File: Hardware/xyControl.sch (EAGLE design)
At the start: 72 parts, among them IC1 ATMEGA2560-16AU, IC2 74HC573D, IC3 K6X4008C1FSMD, IC4 FT232RL, Q7 16M, T1 0-XYTHOBUZ_TASTER

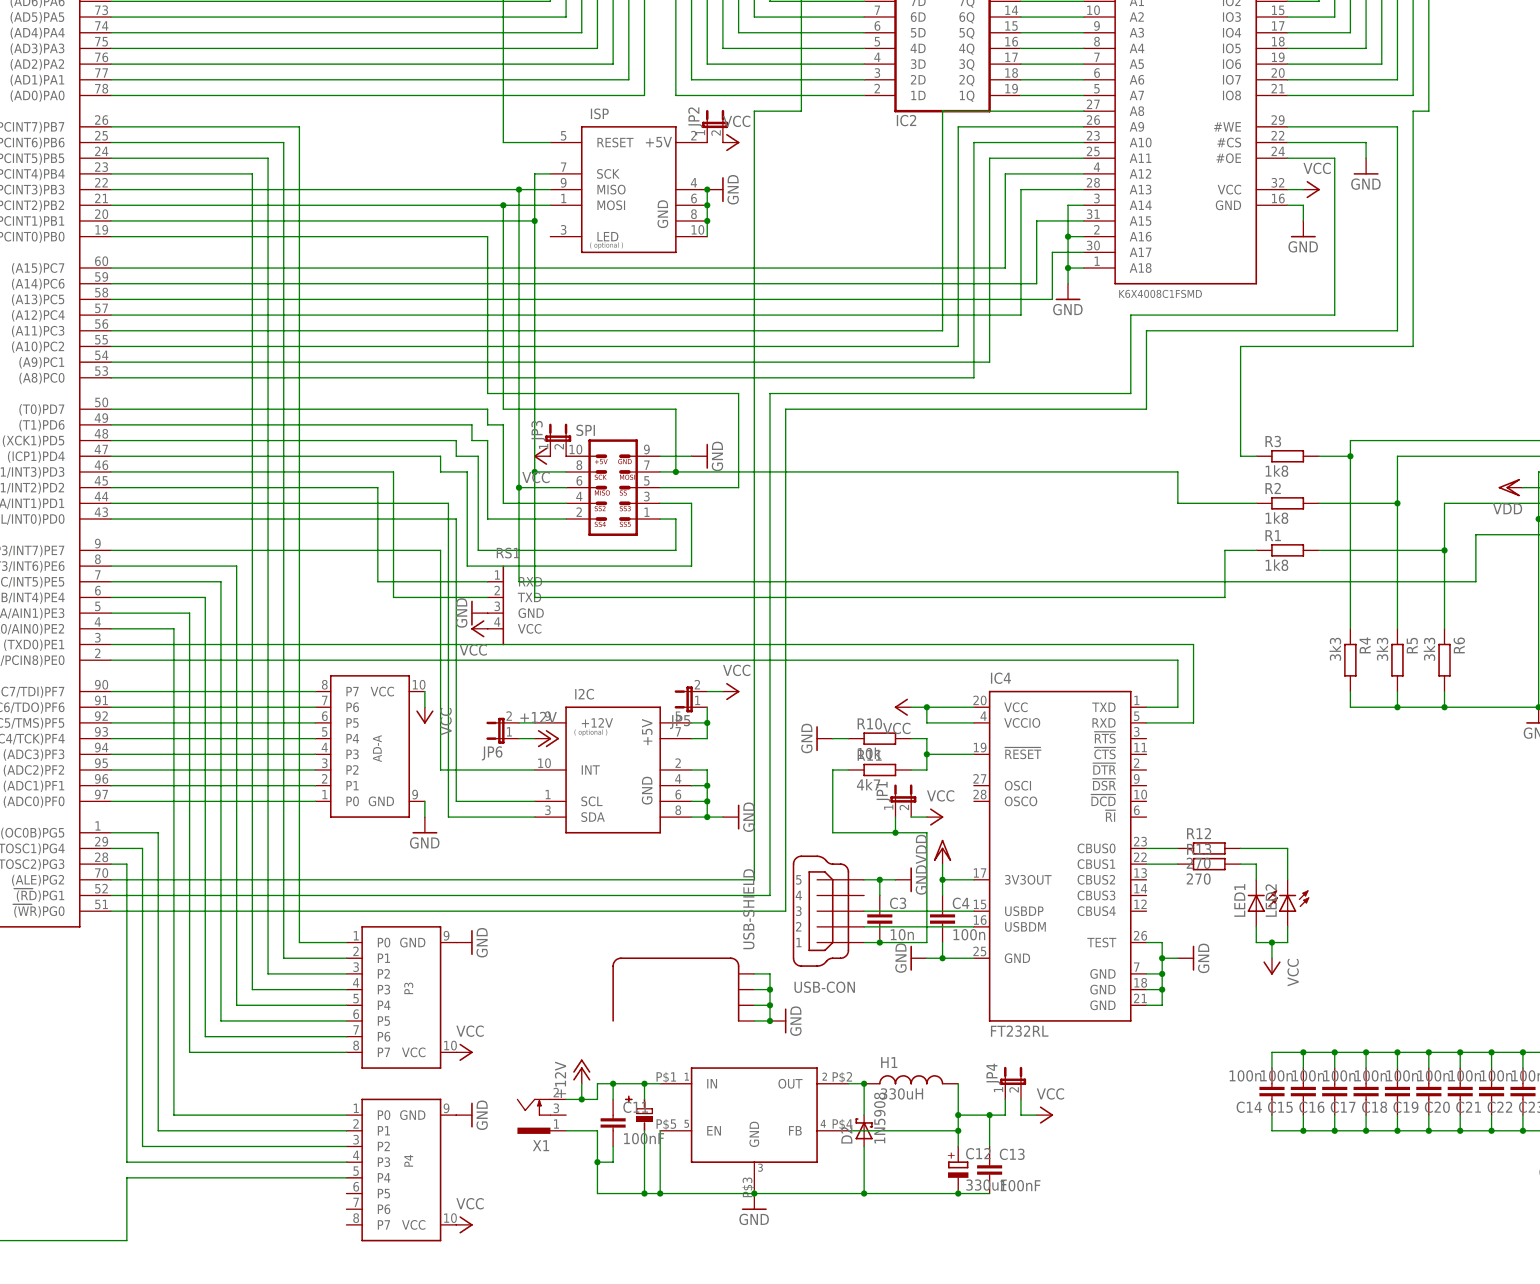
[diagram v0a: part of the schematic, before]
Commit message: Added bank switching.
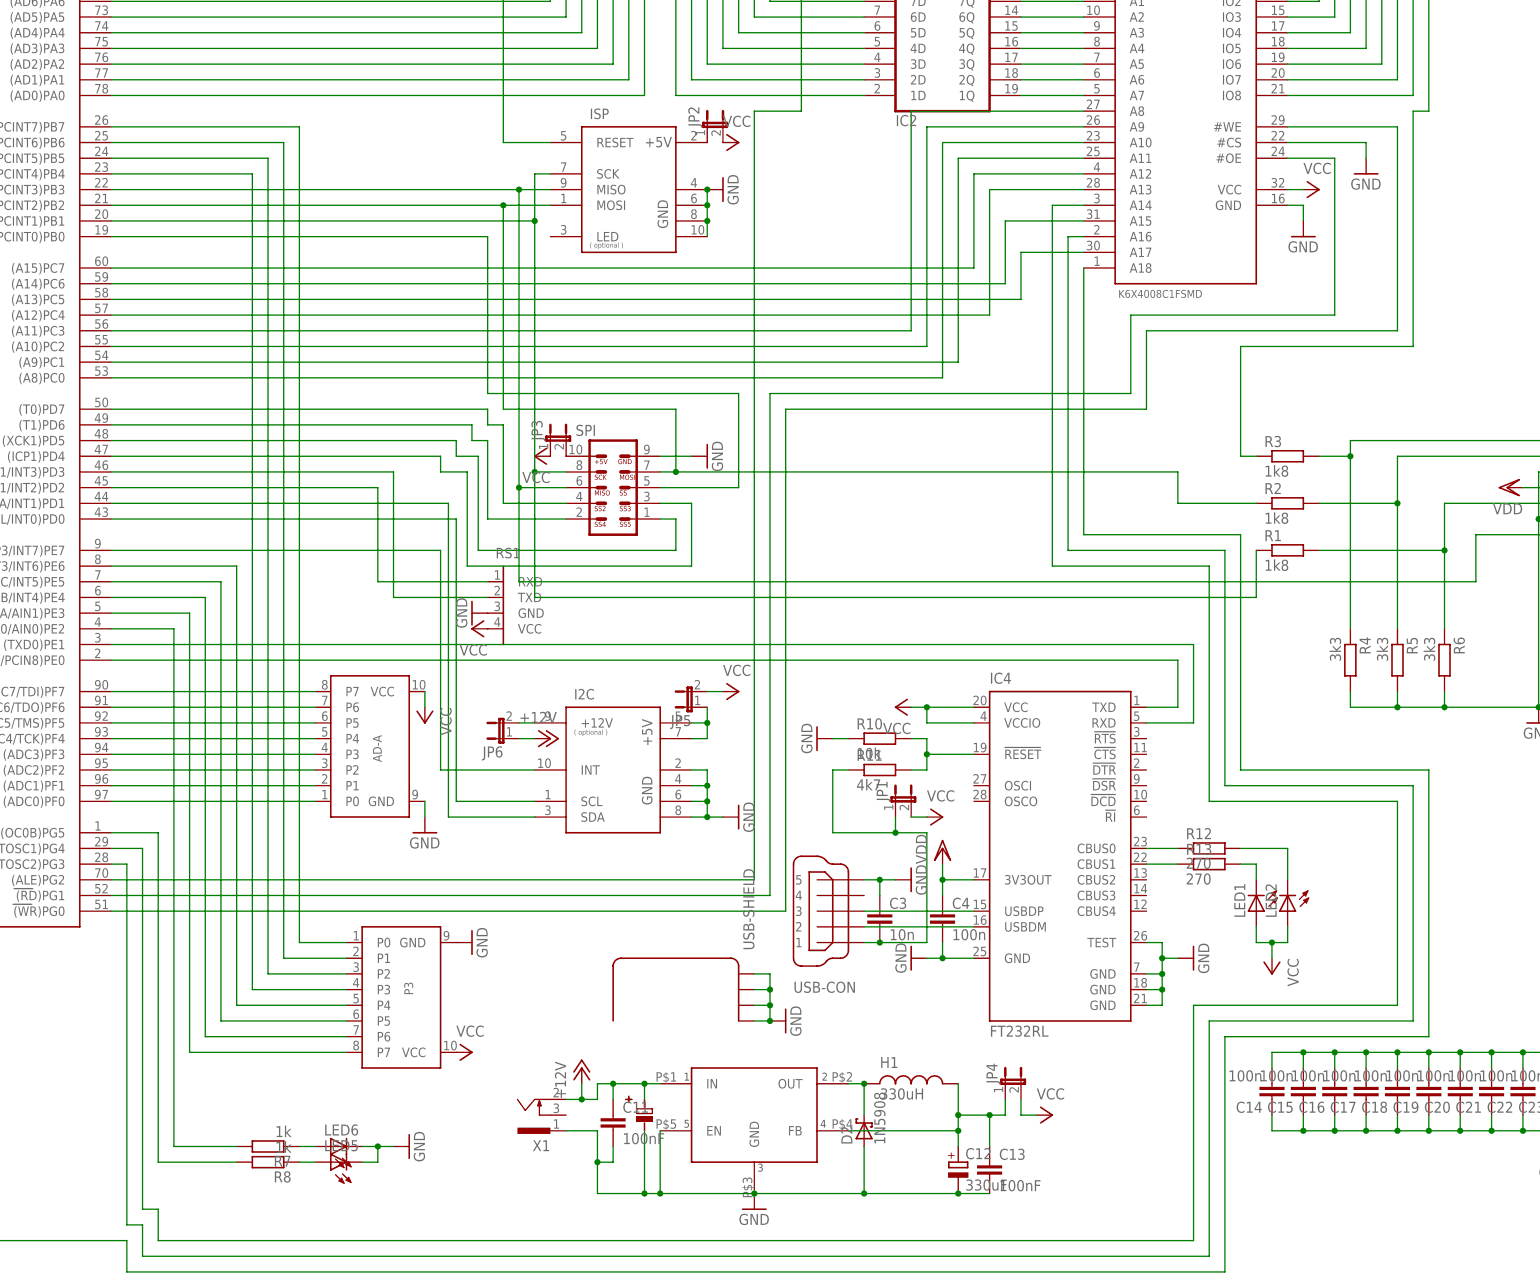
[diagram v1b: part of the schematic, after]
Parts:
- removed P4: (no value), 01-roboternetz-definitionen:PORT
- added LED5, LED6: (no value), led:LEDCHIP-LED0603
- added R7, R8: 1k, resistor:R-EU_R0603
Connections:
- new net N$70: LED6.A, R7.1
- new net N$71: LED5.A, R8.1
- net GND: now also LED5.C, LED6.C; no longer IC3.A14, IC3.A16, IC3.A18, P4.GND
- net N$109: now also IC3.A18; no longer P4.P4
- net N$114: now also R8.2; no longer P4.P1
- net N$115: now also R7.2; no longer P4.P0
- net N$59: now also IC3.A16; no longer P4.P3
- net N$69: now also IC3.A14; no longer P4.P2
- net VCC: no longer P4.VCC

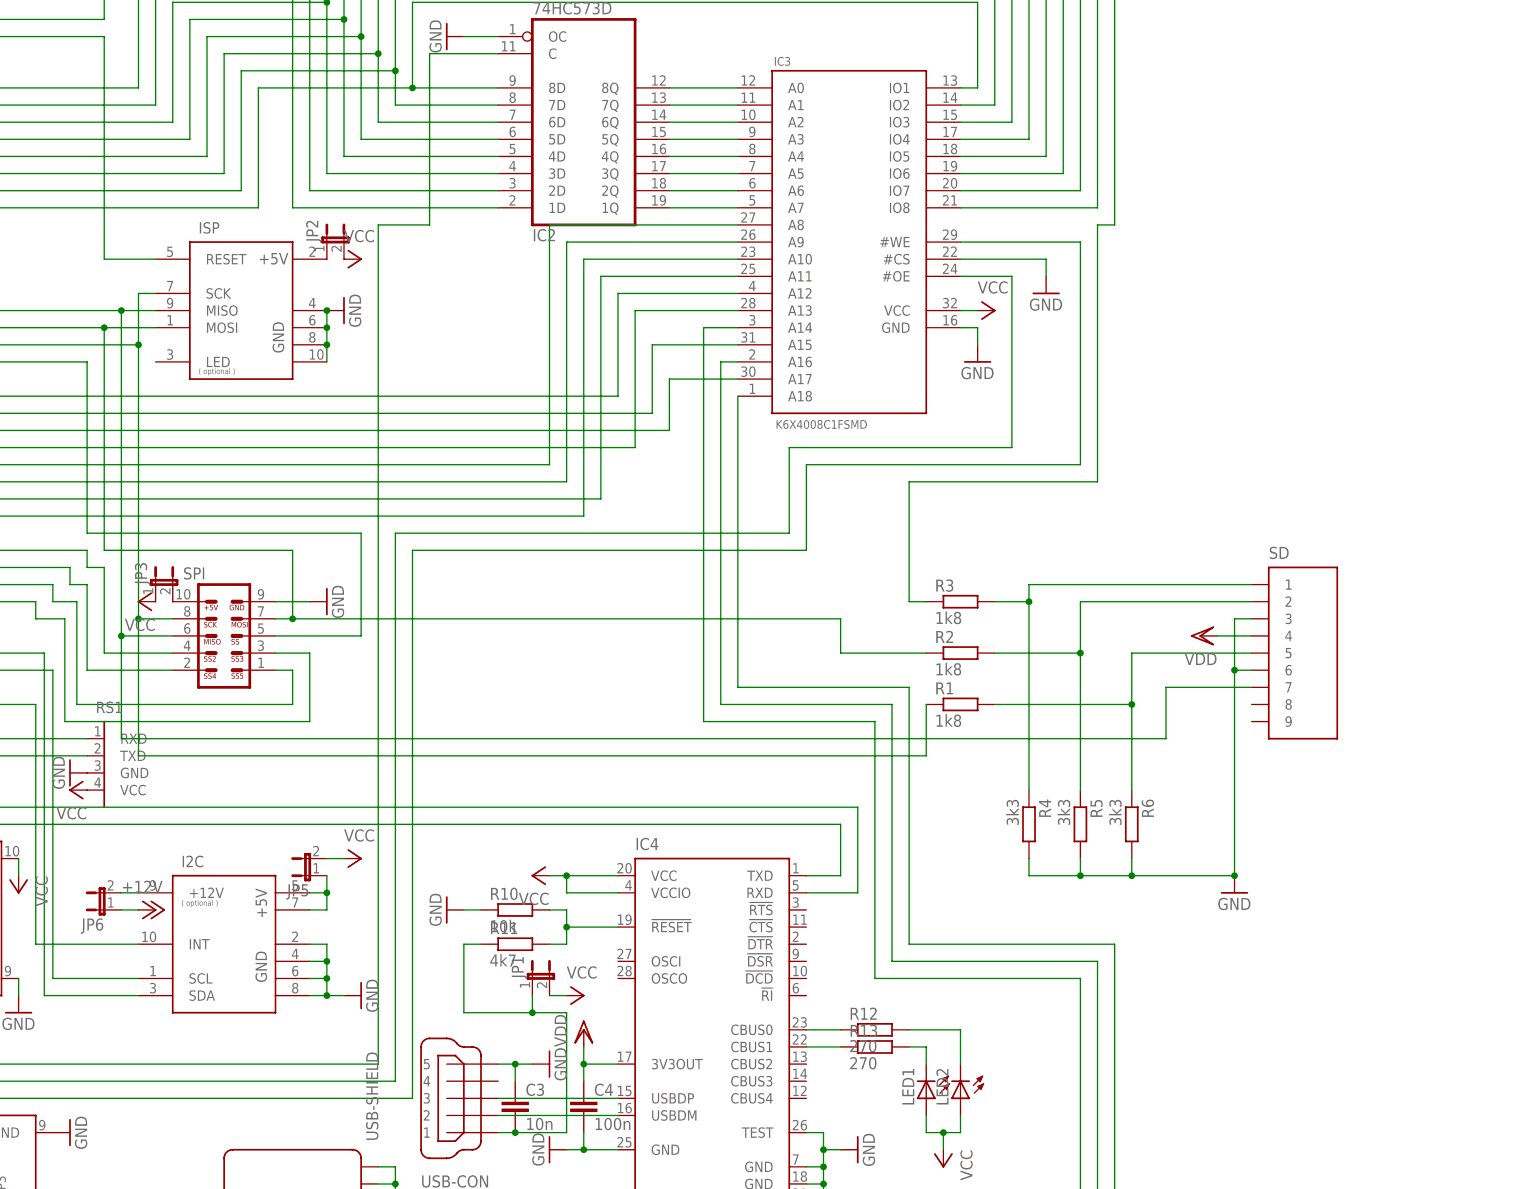
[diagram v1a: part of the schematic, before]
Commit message: New 3V3 Regulator.
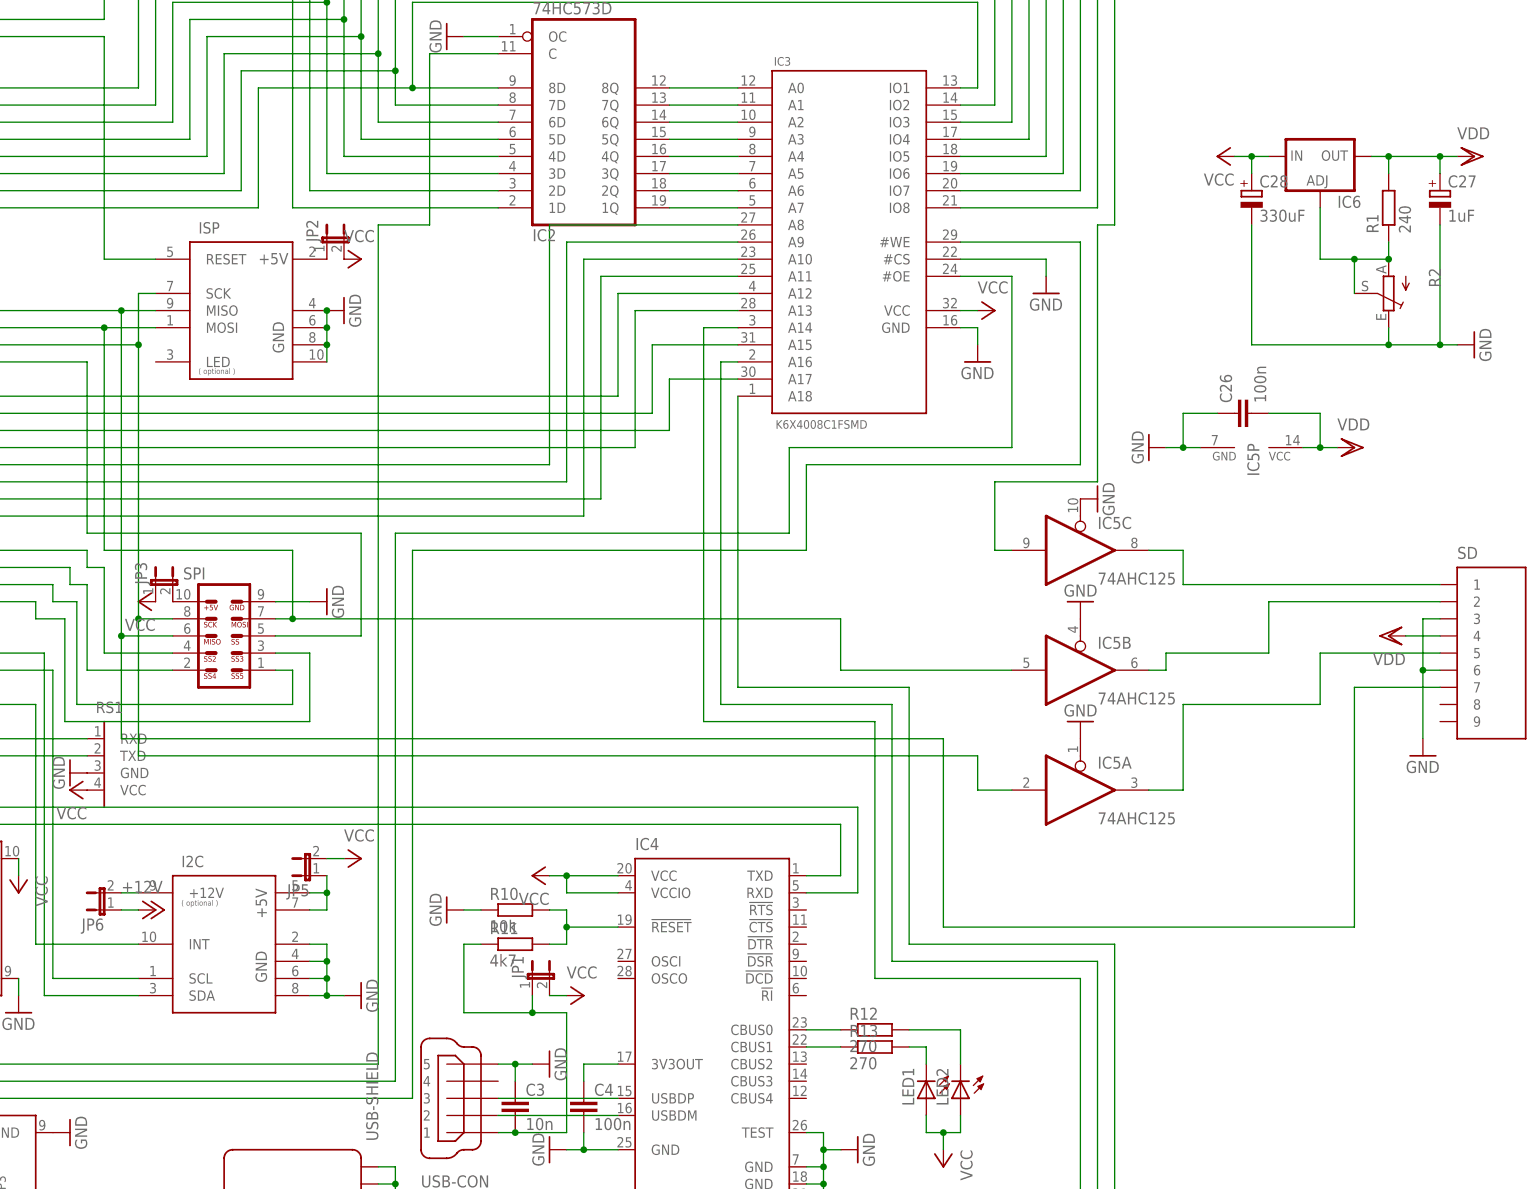
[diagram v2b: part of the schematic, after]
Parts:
- removed R3: 1k8, resistor:R-EU_R0603
- removed R4, R5, R6: 3k3, resistor:R-EU_R0603
- added C26: 100n, resistor:C-EUC0603K
- added C27: 1uF, resistor:CPOL-EUE2.5-6
- added C28: 330uF, resistor:CPOL-EUE5-10.5
- added IC5: 74AHC125, 74xx-eu:74HC125D
- added IC6: (no value), v-reg:LM317L
- R1: value 1k8 -> 240
- R2: value 1k8 -> (none); device resistor:R-EU_R0603 -> LED_Cube:POT_TRIM_EU-ST10
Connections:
- new net N$73: C4.1, IC4.3V3OUT
- new net N$83: IC6.ADJ, R1.1, R2.A, R2.S
- net GND: now also C26.1, C27.-, C28.-, IC5A.OE, IC5B.OE, IC5C.OE, IC5P.GND, R2.E; no longer R4.2, R5.2, R6.2
- net N$37: now also IC5A.I; no longer R1.1
- net N$39: now also IC5B.I; no longer R2.1
- net N$76: now also IC5C.I; no longer R3.1
- net N$77: now also IC5A.O; no longer R1.2, R6.1
- net N$78: now also IC5B.O; no longer R2.2, R5.1
- net N$79: now also IC5C.O; no longer R3.2, R4.1
- net VCC: now also C28.+, IC6.IN
- net VDD: now also C26.2, C27.+, IC5P.VCC, IC6.OUT, R1.2; no longer C4.1, IC4.3V3OUT
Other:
- moved on the sheet: R1, SD
